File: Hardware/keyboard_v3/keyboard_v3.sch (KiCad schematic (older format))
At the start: 19 parts, among them J1 Conn_01x08_Male, SW1 SW_Push, SW2 SW_Push, SW3 SW_Push, SW4 SW_Push, U1 74HC14

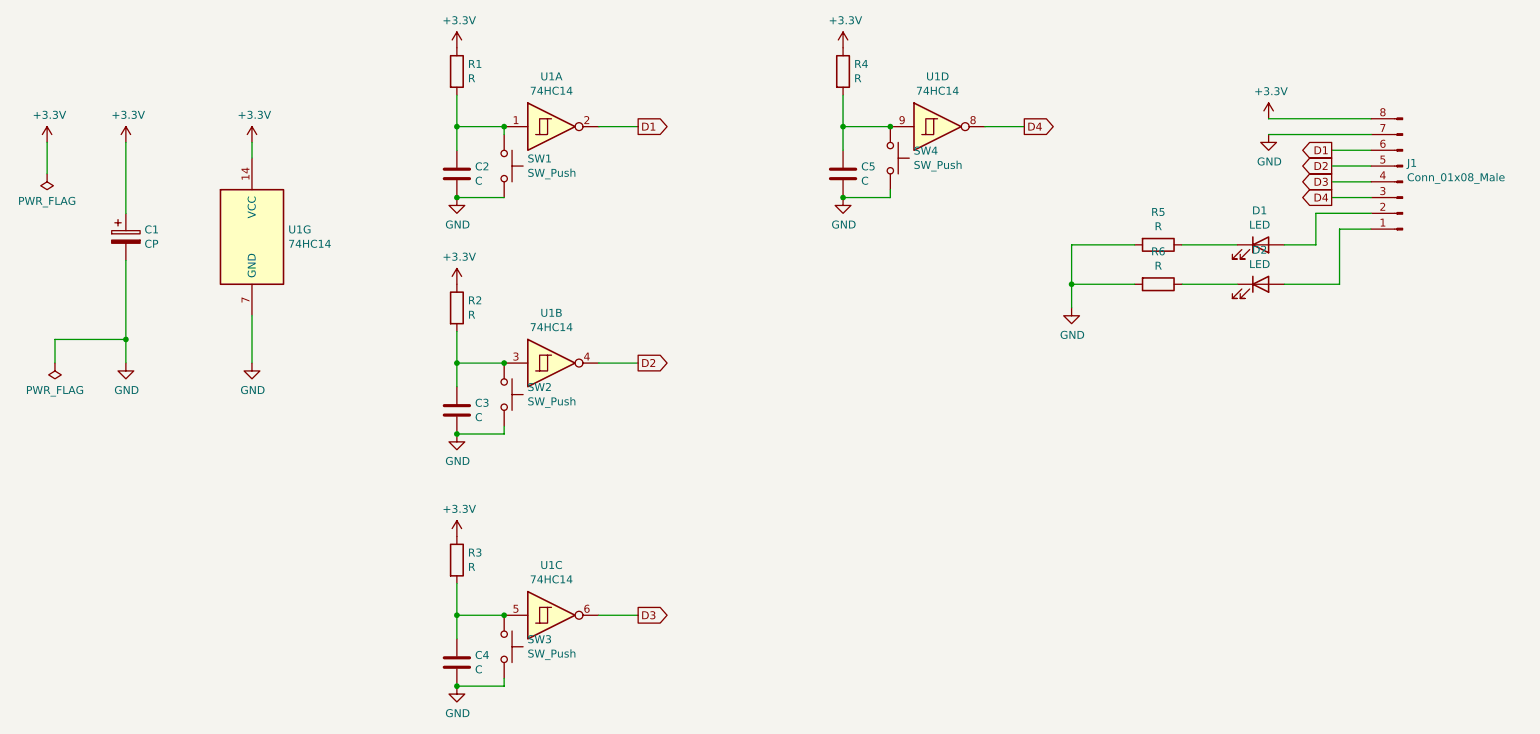
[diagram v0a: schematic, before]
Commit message: Распаян и протестирован модуль клавиатуры keyboard_v3/. Можно приступить к доработке основного приложения
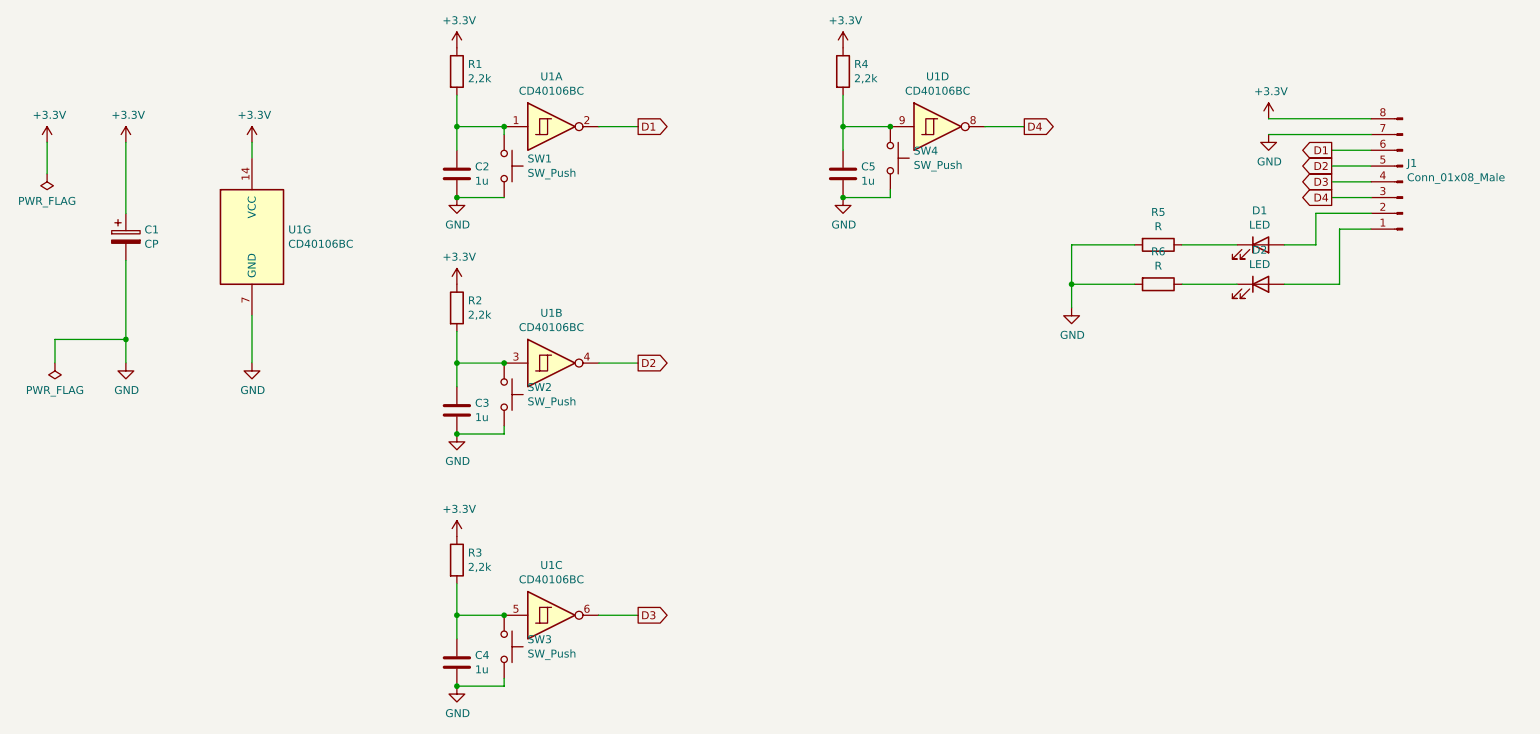
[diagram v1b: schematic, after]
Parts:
- C2, C3, C4, C5: value C -> 1u
- R1, R2, R3, R4: value R -> 2,2k
- U1: value 74HC14 -> CD40106BC
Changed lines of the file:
@@
 P 4150 1700
 F 0 "U1" H 4150 2017 50  0000 C CNN
-F 1 "74HC14" H 4150 1926 50  0000 C CNN
+F 1 "CD40106BC" H 4150 1926 50  0000 C CNN
 F 2 "Package_SO:SOIC-14_3.9x8.7mm_P1.27mm" H 4150 1700 50  0001 C CNN
 F 3 "http://www.ti.com/lit/gpn/sn74HC14" H 4150 1700 50  0001 C CNN
@@
 P 4150 3200
 F 0 "U1" H 4150 3517 50  0000 C CNN
-F 1 "74HC14" H 4150 3426 50  0000 C CNN
+F 1 "CD40106BC" H 4150 3426 50  0000 C CNN
 F 2 "Package_SO:SOIC-14_3.9x8.7mm_P1.27mm" H 4150 3200 50  0001 C CNN
 F 3 "http://www.ti.com/lit/gpn/sn74HC14" H 4150 3200 50  0001 C CNN
@@
 P 4150 4800
 F 0 "U1" H 4150 5117 50  0000 C CNN
-F 1 "74HC14" H 4150 5026 50  0000 C CNN
+F 1 "CD40106BC" H 4150 5026 50  0000 C CNN
 F 2 "Package_SO:SOIC-14_3.9x8.7mm_P1.27mm" H 4150 4800 50  0001 C CNN
 F 3 "http://www.ti.com/lit/gpn/sn74HC14" H 4150 4800 50  0001 C CNN
@@
 P 6600 1700
 F 0 "U1" H 6600 2017 50  0000 C CNN
-F 1 "74HC14" H 6600 1926 50  0000 C CNN
+F 1 "CD40106BC" H 6600 1926 50  0000 C CNN
 F 2 "Package_SO:SOIC-14_3.9x8.7mm_P1.27mm" H 6600 1700 50  0001 C CNN
 F 3 "http://www.ti.com/lit/gpn/sn74HC14" H 6600 1700 50  0001 C CNN
@@
 P 2250 2400
 F 0 "U1" H 2480 2446 50  0000 L CNN
-F 1 "74HC14" H 2480 2355 50  0000 L CNN
+F 1 "CD40106BC" H 2480 2355 50  0000 L CNN
 F 2 "Package_SO:SOIC-14_3.9x8.7mm_P1.27mm" H 2250 2400 50  0001 C CNN
 F 3 "http://www.ti.com/lit/gpn/sn74HC14" H 2250 2400 50  0001 C CNN
@@
 P 3550 1350
 F 0 "R1" H 3620 1396 50  0000 L CNN
-F 1 "R" H 3620 1305 50  0000 L CNN
+F 1 "2,2k" H 3620 1305 50  0000 L CNN
 F 2 "Resistor_SMD:R_1206_3216Metric_Pad1.30x1.75mm_HandSolder" V 3480 1350 50  0001 C CNN
 F 3 "~" H 3550 1350 50  0001 C CNN
@@
 P 3550 2000
 F 0 "C2" H 3665 2046 50  0000 L CNN
-F 1 "C" H 3665 1955 50  0000 L CNN
+F 1 "1u" H 3665 1955 50  0000 L CNN
 F 2 "Capacitor_SMD:C_1206_3216Metric_Pad1.33x1.80mm_HandSolder" H 3588 1850 50  0001 C CNN
 F 3 "~" H 3550 2000 50  0001 C CNN
@@
 P 3550 2850
 F 0 "R2" H 3620 2896 50  0000 L CNN
-F 1 "R" H 3620 2805 50  0000 L CNN
+F 1 "2,2k" H 3620 2805 50  0000 L CNN
 F 2 "Resistor_SMD:R_1206_3216Metric_Pad1.30x1.75mm_HandSolder" V 3480 2850 50  0001 C CNN
 F 3 "~" H 3550 2850 50  0001 C CNN
@@
 P 3550 3500
 F 0 "C3" H 3665 3546 50  0000 L CNN
-F 1 "C" H 3665 3455 50  0000 L CNN
+F 1 "1u" H 3665 3455 50  0000 L CNN
 F 2 "Capacitor_SMD:C_1206_3216Metric_Pad1.33x1.80mm_HandSolder" H 3588 3350 50  0001 C CNN
 F 3 "~" H 3550 3500 50  0001 C CNN
@@
 P 3550 4450
 F 0 "R3" H 3620 4496 50  0000 L CNN
-F 1 "R" H 3620 4405 50  0000 L CNN
+F 1 "2,2k" H 3620 4405 50  0000 L CNN
 F 2 "Resistor_SMD:R_1206_3216Metric_Pad1.30x1.75mm_HandSolder" V 3480 4450 50  0001 C CNN
 F 3 "~" H 3550 4450 50  0001 C CNN
@@
 P 3550 5100
 F 0 "C4" H 3665 5146 50  0000 L CNN
-F 1 "C" H 3665 5055 50  0000 L CNN
+F 1 "1u" H 3665 5055 50  0000 L CNN
 F 2 "Capacitor_SMD:C_1206_3216Metric_Pad1.33x1.80mm_HandSolder" H 3588 4950 50  0001 C CNN
 F 3 "~" H 3550 5100 50  0001 C CNN
@@
 P 6000 1350
 F 0 "R4" H 6070 1396 50  0000 L CNN
-F 1 "R" H 6070 1305 50  0000 L CNN
+F 1 "2,2k" H 6070 1305 50  0000 L CNN
 F 2 "Resistor_SMD:R_1206_3216Metric_Pad1.30x1.75mm_HandSolder" V 5930 1350 50  0001 C CNN
 F 3 "~" H 6000 1350 50  0001 C CNN
@@
 P 6000 2000
 F 0 "C5" H 6115 2046 50  0000 L CNN
-F 1 "C" H 6115 1955 50  0000 L CNN
+F 1 "1u" H 6115 1955 50  0000 L CNN
 F 2 "Capacitor_SMD:C_1206_3216Metric_Pad1.33x1.80mm_HandSolder" H 6038 1850 50  0001 C CNN
 F 3 "~" H 6000 2000 50  0001 C CNN
